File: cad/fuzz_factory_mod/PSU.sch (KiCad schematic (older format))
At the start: 15 parts

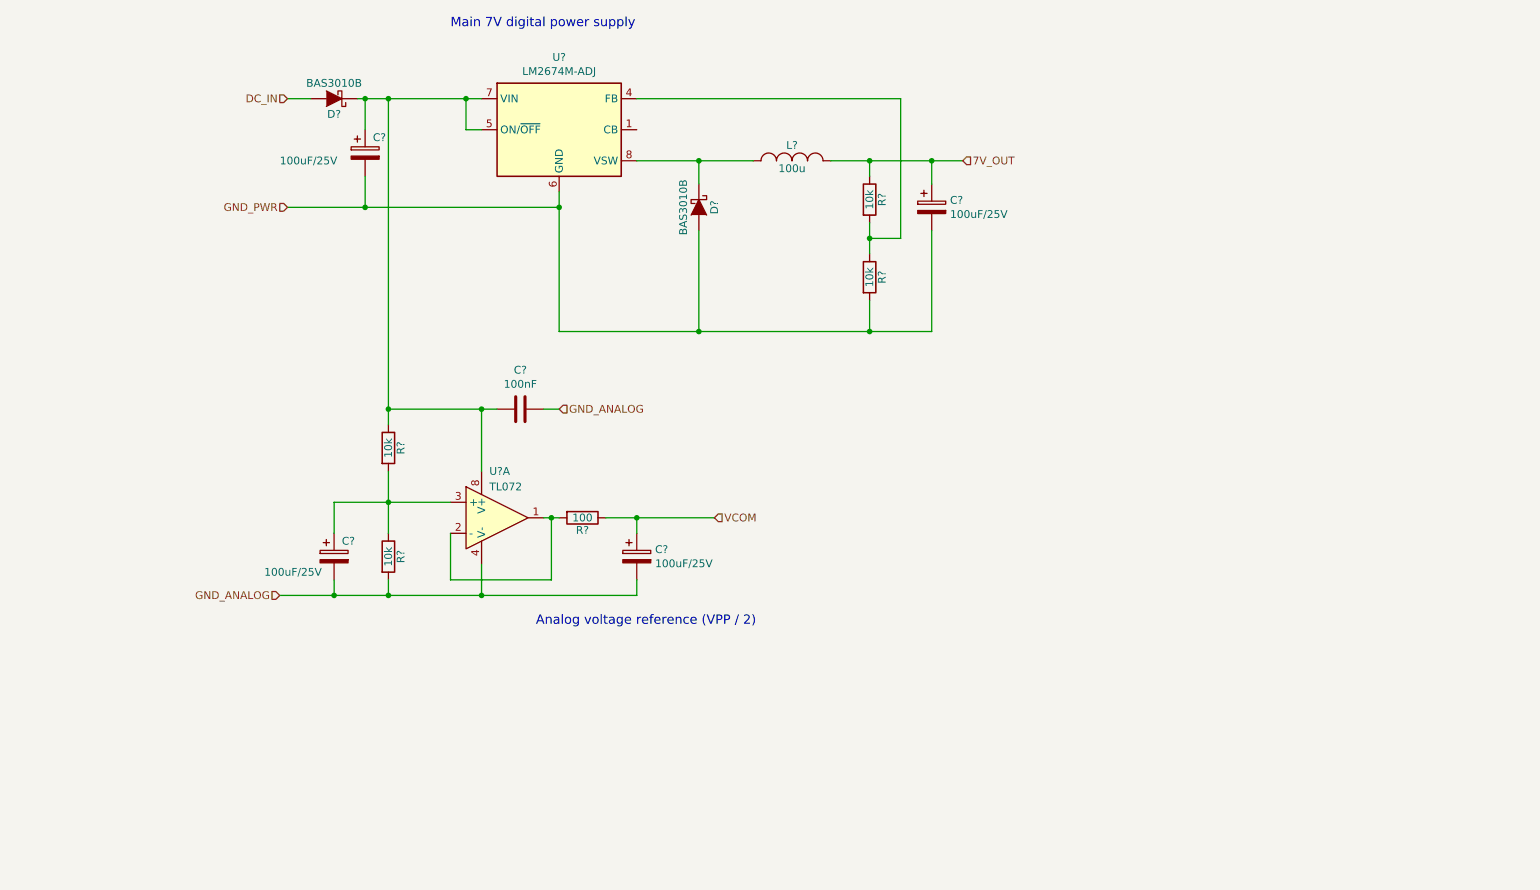
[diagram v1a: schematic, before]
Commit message: Continued schematic.
Modified fuuz_factory circuit : use of matched transistor pairs.
Added USB interface, through FT230X and direct to MCU.
Associated footprints, except for XTAL and trimmers.
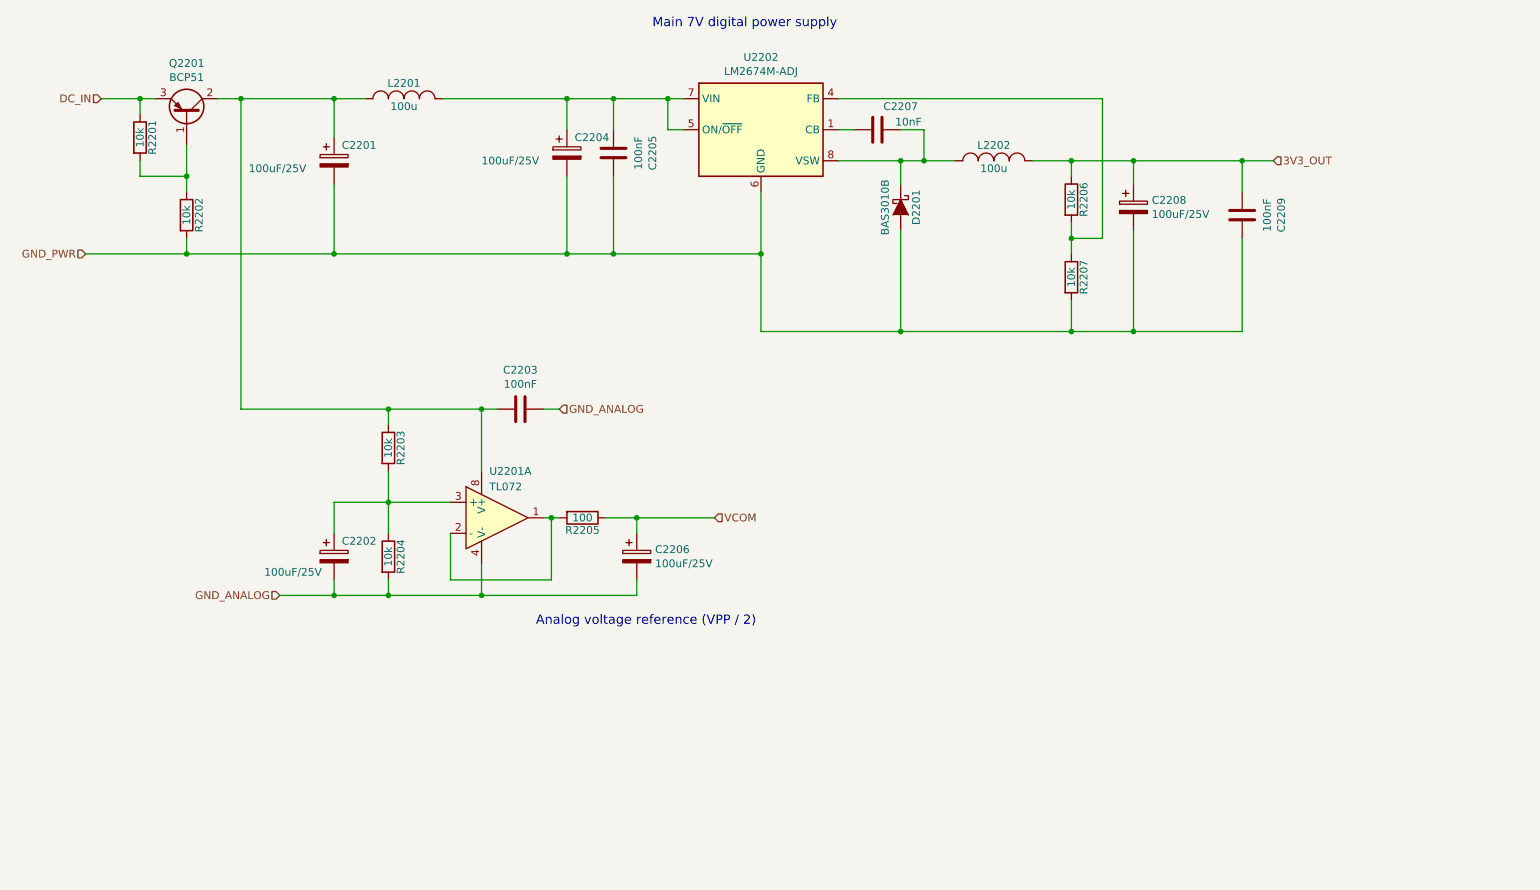
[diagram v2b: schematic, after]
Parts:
- removed D?: BAS3010B, Diodes_SMD:SOD-323, symbol flax_lib:BAS3010B
- added C2201: 100uF/25V, Capacitors_SMD:CP_Elec_6.3x4.5, symbol Device:CP
- added C2205, C2209: 100nF, Capacitors_SMD:C_0603, symbol Device:C
- added C2207: 10nF, Capacitors_SMD:C_0603, symbol Device:C
- added L2201: 100u, flax_lib:L_TDK_SLF7045, symbol flax_lib:SLF7045T-221MR33-PF
- added Q2201: BCP51, Package_TO_SOT_SMD:SOT-223, symbol Transistor_BJT:BCP51
- added R2201, R2202: 10k, Resistors_SMD:R_0603, symbol Device:R
- C2202, C2204, C2206, C2208: renamed from C?; footprint (none) -> Capacitors_SMD:CP_Elec_6.3x4.5
- C2203: renamed from C?; footprint (none) -> Capacitors_SMD:C_0603
- R2203, R2204, R2205, R2206, R2207: renamed from R?; footprint Resistors_SMD:R_0603_HandSoldering -> Resistors_SMD:R_0603
- U2201: renamed from U?; footprint (none) -> Housings_SOIC:SOIC-8_3.9x4.9mm_Pitch1.27mm
- gave numbers to parts that had none: 3
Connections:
- net DC_IN: now also Q2201.3 (E), R2201.1
- net GND_PWR: now also C2201.2, C2205.2, C2209.2, R2202.2
- net at D2201.1 (K), L2202.1, U2202.8 (VSW): now also C2207.2
- net at C2203.1, R2203.1, U2201.8 (V+): now also C2201.1, L2201.1, Q2201.2 (C); no longer C2204.1, U2202.5 (ON/~OFF), U2202.7 (VIN)
- net at U2202.1 (CB): now also C2207.1
- net 7V_OUT renamed 3V3_OUT
- net 3V3_OUT: now also C2209.1
- new net: C2204.1, C2205.1, L2201.2, U2202.5 (ON/~OFF), U2202.7 (VIN)
- new net: Q2201.1 (B), R2201.2, R2202.1
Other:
- moved on the sheet: C2204, C2208, D2201, L2202, R2206, R2207, U2202

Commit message: Continued schematic.
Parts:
- D2201: footprint Diodes_SMD:SOD-323 -> Diodes_SMD:D_SOD-323
- Q2201: footprint Package_TO_SOT_SMD:SOT-223 -> TO_SOT_Packages_SMD:SOT-223
- U2202: footprint Package_SO:SOIC-8_3.9x4.9mm_P1.27mm -> Housings_SOIC:SOIC-8_3.9x4.9mm_Pitch1.27mm
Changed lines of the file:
@@
 $Descr A4 11693 8268
 encoding utf-8
-Sheet 21 22
+Sheet 25 26
 Title ""
 Date ""
@@
 F 0 "D2201" H 6300 2300 50  0000 C CNN
 F 1 "BAS3010B" H 6300 2100 50  0000 C CNN
-F 2 "Diodes_SMD:SOD-323" H 6300 2200 50  0001 C CNN
+F 2 "Diodes_SMD:D_SOD-323" H 6300 2200 50  0001 C CNN
 F 3 "" H 6300 2200 50  0000 C CNN
 	1    6300 2200
@@
 F 0 "U2202" H 5400 2167 50  0000 C CNN
 F 1 "LM2674M-ADJ" H 5400 2076 50  0000 C CNN
-F 2 "Package_SO:SOIC-8_3.9x4.9mm_P1.27mm" H 5450 1350 50  0001 L CIN
+F 2 "Housings_SOIC:SOIC-8_3.9x4.9mm_Pitch1.27mm" H 5450 1350 50  0001 L CIN
 F 3 "http://www.ti.com/lit/ds/symlink/lm2674.pdf" H 5400 1700 50  0001 C CNN
 	1    5400 1700
@@
 F 0 "Q2201" V 2028 1600 50  0000 C CNN
 F 1 "BCP51" V 1937 1600 50  0000 C CNN
-F 2 "Package_TO_SOT_SMD:SOT-223" H 1900 1525 50  0001 L CIN
+F 2 "TO_SOT_Packages_SMD:SOT-223" H 1900 1525 50  0001 L CIN
 F 3 "http://www.fairchildsemi.com/ds/BC/BCP51.pdf" H 1700 1600 50  0001 L CNN
 	1    1700 1600

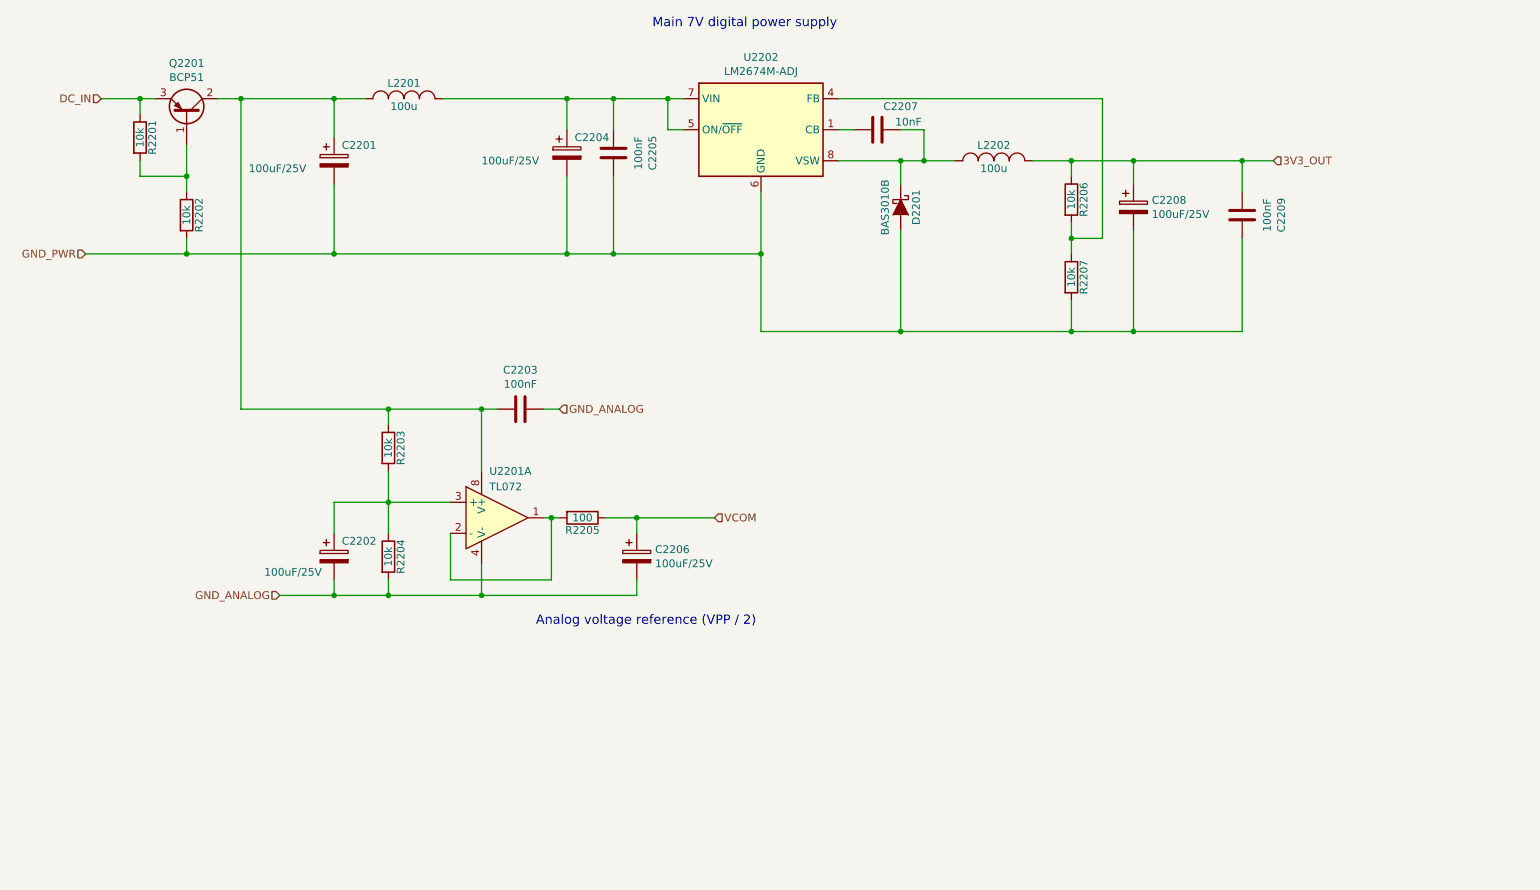
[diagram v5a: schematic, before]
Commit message: Changes architecture.
Corrections on schematic.
Continued Layout placement.
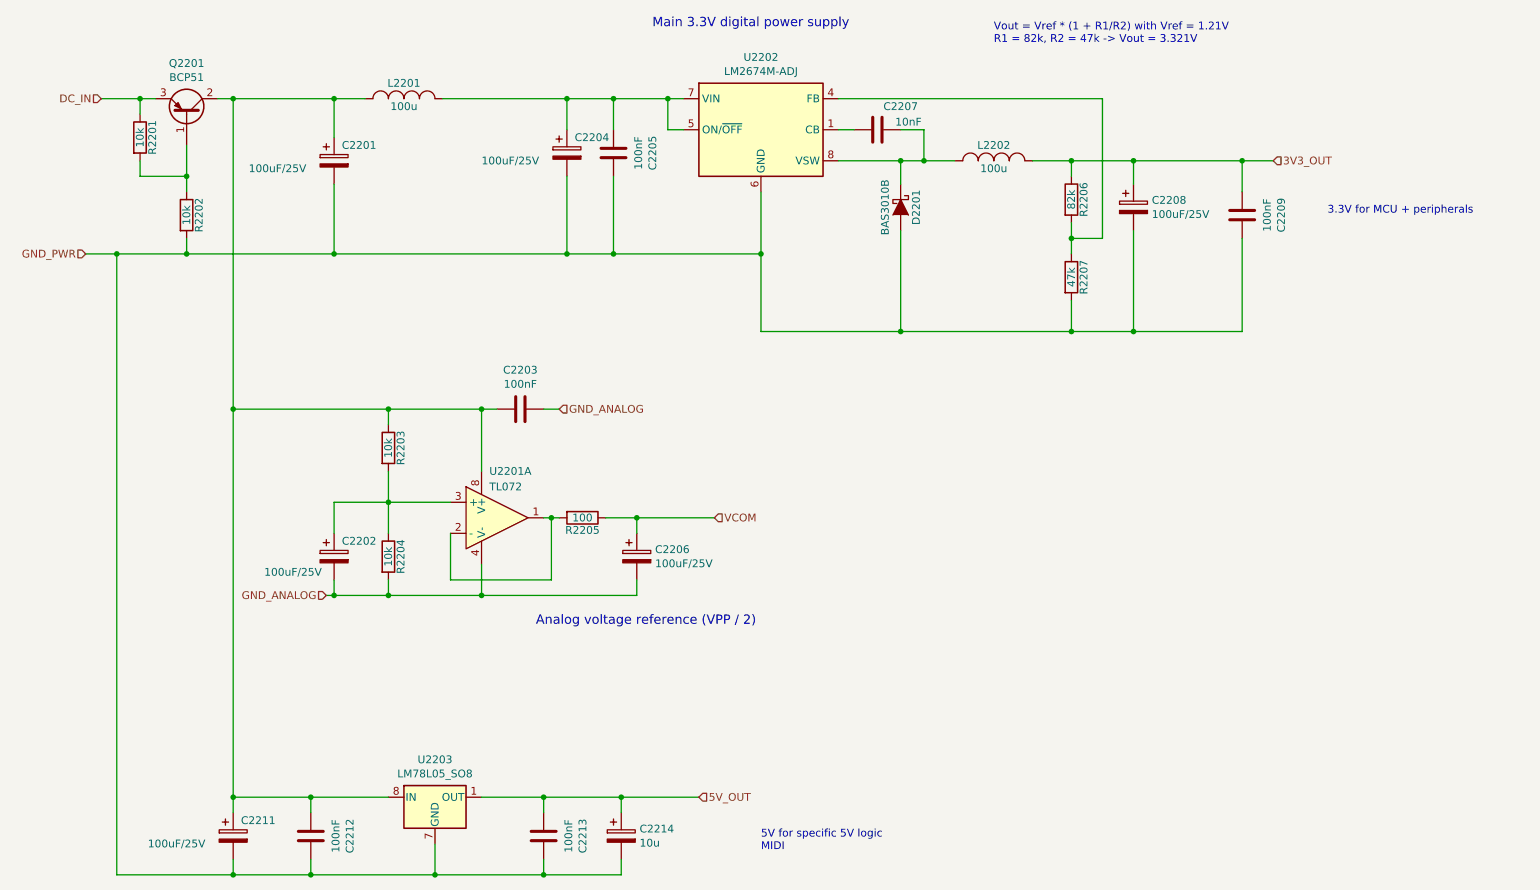
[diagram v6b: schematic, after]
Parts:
- added C2211: 100uF/25V, Capacitors_SMD:CP_Elec_6.3x4.5, symbol Device:CP
- added C2212, C2213: 100nF, Capacitors_SMD:C_0603, symbol Device:C
- added C2214: 10u, Capacitors_SMD:CP_Elec_6.3x4.5, symbol Device:CP
- added U2203: LM78L05_SO8, Housings_SOIC:SOIC-8_3.9x4.9mm_Pitch1.27mm, symbol Regulator_Linear:LM78L05_SO8
- R2206: value 10k -> 82k
- R2207: value 10k -> 47k
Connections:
- net GND_PWR: now also C2211.2, C2212.2, C2213.2, C2214.2, U2203.2 (GND), U2203.3 (GND), U2203.6 (GND), U2203.7 (GND)
- net at C2201.1, C2203.1, L2201.1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: now also C2211.1, C2212.1, U2203.8 (IN)
- new net 5V_OUT: C2213.1, C2214.1, U2203.1 (OUT)
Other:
- note added: "3.3V for MCU + peripherals"
- note added: "5V for specific 5V logic\nMIDI"
- note added: "Main 3.3V digital power supply"
- note added: "Vout = Vref * (1 + R1/R2) with Vref = 1.21V\nR1 = 82k, R2 = 47k -> Vout = 3.321V"
- note removed: "Main 7V digital power supply"
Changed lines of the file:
@@
 $Descr A4 11693 8268
 encoding utf-8
-Sheet 30 30
+Sheet 22 22
 Title ""
 Date ""
@@
 Connection ~ 4600 4200
 Text Notes 4700 1050 0    60   ~ 0
-Main 7V digital power supply
+Main 3.3V digital power supply
 Text Notes 3950 4900 0    60   ~ 0
 Analog voltage reference (VPP / 2)
@@
 Text HLabel 5100 4200 2    50   Input ~ 0
 VCOM
-Text HLabel 2300 4700 0    50   Input ~ 0
+Text HLabel 2600 4700 0    50   Input ~ 0
 GND_ANALOG
 $Comp
@@
 Connection ~ 7800 1900
 Wire Wire Line
-	2650 4700 2300 4700
-Connection ~ 2650 4700
-Wire Wire Line
 	5100 4200 4600 4200
 $Comp
@@
 P 7400 2150
 F 0 "R2206" V 7480 2150 50  0000 C CNN
-F 1 "10k" V 7400 2150 50  0000 C CNN
+F 1 "82k" V 7400 2150 50  0000 C CNN
 F 2 "Resistors_SMD:R_0603" V 7330 2150 50  0001 C CNN
 F 3 "" H 7400 2150 50  0000 C CNN
@@
 P 7400 2650
 F 0 "R2207" V 7480 2650 50  0000 C CNN
-F 1 "10k" V 7400 2650 50  0000 C CNN
+F 1 "47k" V 7400 2650 50  0000 C CNN
 F 2 "Resistors_SMD:R_0603" V 7330 2650 50  0001 C CNN
 F 3 "" H 7400 2650 50  0000 C CNN
@@
 	1700 2000 1700 2100
 Wire Wire Line
-	1900 1500 2050 1500
-Wire Wire Line
-	1050 2500 1700 2500
+	1900 1500 2000 1500
+Wire Wire Line
+	1050 2500 1250 2500
 Wire Wire Line
 	1700 2400 1700 2500
@@
 Wire Wire Line
 	4150 1500 4450 1500
-Wire Wire Line
-	3000 3500 2050 3500
-Wire Wire Line
-	2050 3500 2050 1500
 Connection ~ 3000 3500
 Wire Wire Line
@@
 Wire Wire Line
 	2850 1500 2650 1500
-Connection ~ 2050 1500
 $Comp
 L Device:CP C2201
@@
 Connection ~ 2650 1500
 Wire Wire Line
-	2650 1500 2050 1500
-Wire Wire Line
 	2650 2050 2650 2500
 Connection ~ 2650 2500
 Wire Wire Line
 	2650 2500 4150 2500
+Text Notes 6900 1150 0    50   ~ 0
+Vout = Vref * (1 + R1/R2) with Vref = 1.21V\nR1 = 82k, R2 = 47k -> Vout = 3.321V
+$Comp
+L Regulator_Linear:LM78L05_SO8 U2203
+U 1 1 5F125F0F
+P 3300 6000
+F 0 "U2203" H 3300 6242 50  0000 C CNN
+F 1 "LM78L05_SO8" H 3300 6151 50  0000 C CNN
+F 2 "Housings_SOIC:SOIC-8_3.9x4.9mm_Pitch1.27mm" H 3400 6200 50  0001 C CIN
+F 3 "http://www.fairchildsemi.com/ds/LM/LM78L05A.pdf" H 3500 6000 50  0001 C CNN
+	1    3300 6000
+	1    0    0    -1
+$EndComp
+$Comp
+L Device:CP C2211
+U 1 1 5F1281A1
+P 2000 6250
+F 0 "C2211" H 2050 6350 50  0000 L CNN
+F 1 "100uF/25V" H 1450 6200 50  0000 L CNN
+F 2 "Capacitors_SMD:CP_Elec_6.3x4.5" H 2038 6100 50  0001 C CNN
+F 3 "~" H 2000 6250 50  0001 C CNN
+	1    2000 6250
+	1    0    0    -1
+$EndComp
+$Comp
+L Device:C C2213
+U 1 1 5F12A37F
+P 4000 6250
+F 0 "C2213" V 4252 6250 50  0000 C CNN
+F 1 "100nF" V 4161 6250 50  0000 C CNN
+F 2 "Capacitors_SMD:C_0603" H 4038 6100 50  0001 C CNN
+F 3 "~" H 4000 6250 50  0001 C CNN
+	1    4000 6250
+	1    0    0    -1
+$EndComp
+$Comp
+L Device:CP C?
+U 1 1 5F13D27B
+P 4500 6250
+AR Path="/5DE4AD88/5DF28E5E/5F13D27B" Ref="C?"  Part="1"
+AR Path="/5DE4AD88/5ED499CE/5F13D27B" Ref="C?"  Part="1"
+AR Path="/5E2FAB43/5F13D27B" Ref="C2214"  Part="1"
+F 0 "C2214" H 4618 6296 50  0000 L CNN
+F 1 "10u" H 4618 6205 50  0000 L CNN
+F 2 "Capacitors_SMD:CP_Elec_6.3x4.5" H 4538 6100 50  0001 C CNN
+F 3 "~" H 4500 6250 50  0001 C CNN
+	1    4500 6250
+	1    0    0    -1
+$EndComp
+Wire Wire Line
+	3600 6000 4000 6000
+Wire Wire Line
+	4000 6000 4000 6100
+Wire Wire Line
+	4000 6000 4500 6000
+Wire Wire Line
+	4500 6000 4500 6100
+Connection ~ 4000 6000
+Wire Wire Line
+	3300 6300 3300 6500
+Wire Wire Line
+	3300 6500 4000 6500
+Wire Wire Line
+	4000 6500 4000 6400
+Wire Wire Line
+	4500 6400 4500 6500
+Wire Wire Line
+	4500 6500 4000 6500
+Connection ~ 4000 6500
+Wire Wire Line
+	2000 6500 2000 6400
+Wire Wire Line
+	2500 6000 2000 6000
+Wire Wire Line
+	2000 6000 2000 6100
+$Comp
+L Device:C C2212
+U 1 1 5F1515BD
+P 2500 6250
+F 0 "C2212" V 2752 6250 50  0000 C CNN
+F 1 "100nF" V 2661 6250 50  0000 C CNN
+F 2 "Capacitors_SMD:C_0603" H 2538 6100 50  0001 C CNN
+F 3 "~" H 2500 6250 50  0001 C CNN
+	1    2500 6250
+	1    0    0    -1
+$EndComp
+Wire Wire Line
+	2500 6100 2500 6000
+Wire Wire Line
+	3000 6000 2500 6000
+Connection ~ 2500 6000
+Wire Wire Line
+	2500 6400 2500 6500
+Connection ~ 2500 6500
+Wire Wire Line
+	2500 6500 2000 6500
+Wire Wire Line
+	2500 6500 3300 6500
+Connection ~ 3300 6500
+Connection ~ 2000 1500
+Wire Wire Line
+	2000 1500 2650 1500
+Wire Wire Line
+	2000 1500 2000 3500
+Wire Wire Line
+	2000 3500 3000 3500
+Connection ~ 2000 3500
+Wire Wire Line
+	2000 3500 2000 6000
+Connection ~ 2000 6000
+Wire Wire Line
+	1250 2500 1250 6500
+Wire Wire Line
+	1250 6500 2000 6500
+Connection ~ 1250 2500
+Wire Wire Line
+	1250 2500 1700 2500
+Connection ~ 2000 6500
+Wire Wire Line
+	2650 4700 2600 4700
+Connection ~ 2650 4700
+Text HLabel 5000 6000 2    50   Input ~ 0
+5V_OUT
+Wire Wire Line
+	5000 6000 4500 6000
+Connection ~ 4500 6000
+Text Notes 9050 2250 0    50   ~ 0
+3.3V for MCU + peripherals
+Text Notes 5400 6350 0    50   ~ 0
+5V for specific 5V logic\nMIDI
 $EndSCHEMATC
